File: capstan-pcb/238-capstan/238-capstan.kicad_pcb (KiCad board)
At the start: 2 copper layers, 58 x 67 mm, 53 parts, among them CN1 CN1, IC1 BA6303F, IC2 4013, IC3 BA6411, J1 0, J2 0

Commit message: Capstan pcb v2024-08-04
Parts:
- moved C6 2.99 mm to (123.3, 81.1)
- moved J2 2.41 mm to (160.5, 81.2)
- moved R2 1.56 mm to (160.5, 77.2), turned to 180 degrees
- moved TP2 1.30 mm to (165.8, 76.2)
- moved JP3 1.09 mm to (165.7, 80.3)
- moved IC2 0.45 mm to (166.6, 88.0)
- renumbered C11 to C10, C10 to C11
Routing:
- net Net-(C3-Pad2): track 68.1 -> 70.0 mm
- net Net-(C5-Pad2): track 9.56 -> 7.68 mm
- net Net-(R2-Pad2): track 4.02 -> 3.15 mm
- net Net-(CN1-Pad3): track 21.2 -> 20.4 mm
- net Net-(IC2-Pad1): track 40.2 -> 40.8 mm
- added copper zone on F.Cu, net GND
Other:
- board text added: "denis@238pro.com v2024-08-04"
- board text removed: "denis@238pro.com v2024-08-03"

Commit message: Capstan PCB v2024-08-06
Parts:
- moved R7 12.7 mm to (165.7, 96.5)
- moved JP2 11.3 mm to (161.2, 97.8)
- moved R8 4.53 mm to (168.8, 102.8)
- moved C3 4.30 mm to (160.8, 106.2)
- moved J1 2.51 mm to (168.8, 100.0)
- moved R9 0.60 mm to (170.2, 96.0)
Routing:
- net Net-(IC1-Pad11): track 22.8 -> 41.4 mm
- net Net-(IC2-Pad1): track 40.8 -> 23.1 mm
- net GND: track 201.3 -> 193.0 mm
- net Net-(J1-Pad2): track 10.2 -> 3.50 mm
- net Net-(IC1-Pad6): track 62.9 -> 56.7 mm
- net Net-(PC1-Pad3): track 8.59 -> 3.55 mm
- net Net-(C3-Pad2): track 70.0 -> 72.0 mm
- net Net-(J1-Pad1): track 5.15 -> 3.40 mm
- net +9V: track 70.9 -> 70.4 mm
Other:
- board text added: "denis@238pro.com v2024-08-06"
- board text removed: "denis@238pro.com v2024-08-04"

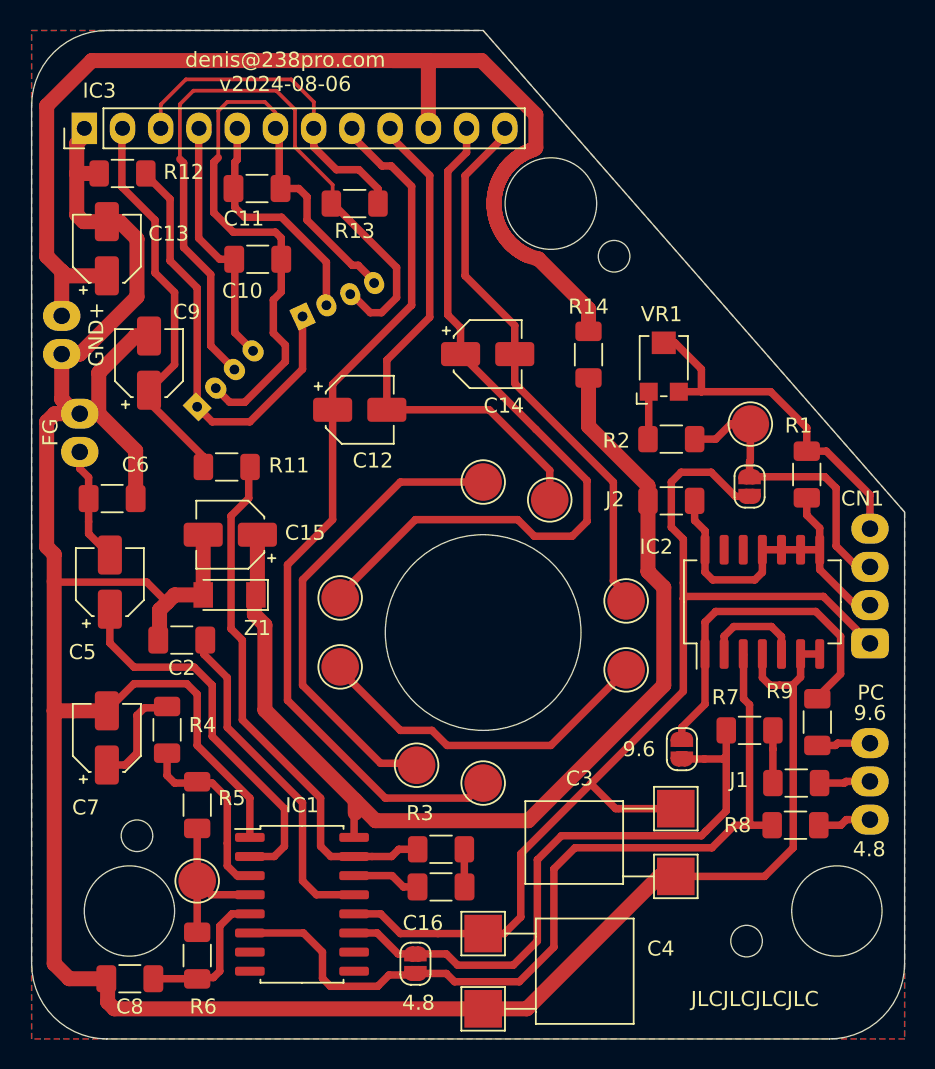
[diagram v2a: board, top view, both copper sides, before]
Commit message: Capstan PCB v2024-08-06 pour +12V
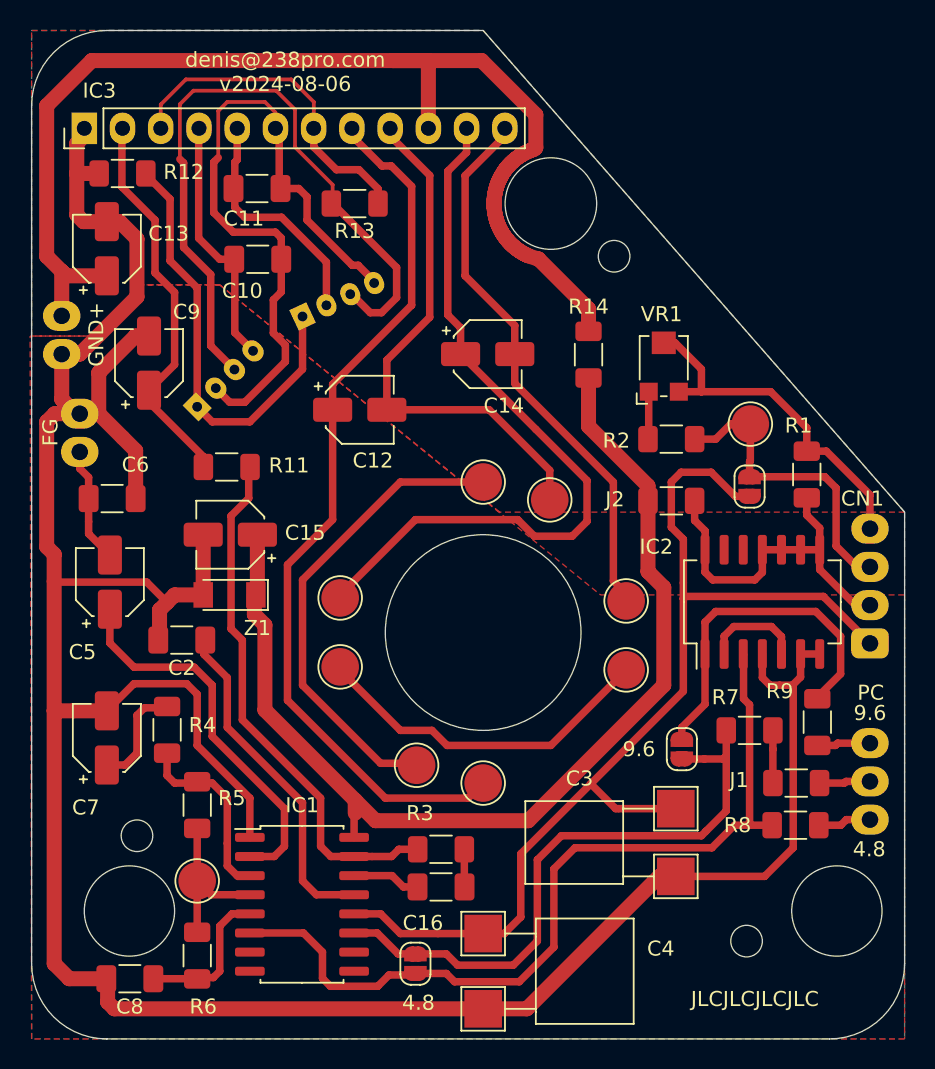
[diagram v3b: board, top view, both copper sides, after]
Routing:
- added copper zone on F.Cu, net +12V
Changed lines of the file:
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@@
   (layers
     (0 F.Cu signal)
-    (31 B.Cu signal)
+    (31 B.Cu signal hide)
     (32 B.Adhes user)
     (33 F.Adhes user hide)
@@
     )
   )
-  (zone (net 1) (net_name GND) (layer F.Cu) (hatch edge 0.508)
-    (connect_pads (clearance 0.508))
-    (min_thickness 0.254)
-    (fill yes (arc_segments 32) (thermal_gap 0.508) (thermal_bridge_width 0.508))
-    (polygon
-      (pts
-        (xy 176 82) (xy 176 117) (xy 118 117) (xy 118 50) (xy 148 50)
-      )
-    )
-  )
   (zone (net 0) (net_name "") (layer F.Cu) (hatch edge 0.508)
     (connect_pads (clearance 0.508))
@@
       )
     )
+  )
+  (zone (net 1) (net_name GND) (layer F.Cu) (hatch edge 0.508)
+    (connect_pads (clearance 0.508))
+    (min_thickness 0.254)
+    (fill yes (arc_segments 32) (thermal_gap 0.508) (thermal_bridge_width 0.508))
+    (polygon
+      (pts
+        (xy 130.5 66.9) (xy 155.8 87.5) (xy 176 87.5) (xy 176 117) (xy 118 117)
+        (xy 117.9 70.3) (xy 122.5 70.3) (xy 125.1 66.9)
+      )
+    )
+  )
+  (zone (net 13) (net_name +12V) (layer F.Cu) (hatch edge 0.508)
+    (connect_pads (clearance 0.508))
+    (min_thickness 0.254)
+    (fill yes (arc_segments 32) (thermal_gap 0.508) (thermal_bridge_width 0.508))
+    (polygon
+      (pts
+        (xy 176 82) (xy 149.1 82) (xy 130.5 66.9) (xy 125.1 66.9) (xy 122.5 70.3)
+        (xy 118 70.3) (xy 118 50) (xy 148 50)
+      )
+    )
